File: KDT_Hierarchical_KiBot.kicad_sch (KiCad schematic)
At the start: 0 parts

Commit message: QR Code Added
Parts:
- added QR1: QR_Revision, ProjectQR:QR_Revision, symbol ProjectQR:QR_Revision
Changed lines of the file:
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@@
+		)
+	)
+	(symbol
+		(lib_id "ProjectQR:QR_Revision")
+		(at 209.55 269.24 0)
+		(unit 1)
+		(exclude_from_sim no)
+		(in_bom no)
+		(on_board yes)
+		(dnp no)
+		(fields_autoplaced yes)
+		(property "Reference" "QR1"
+			(at 209.55 256.54 0)
+			(effects
+				(font
+					(size 1.27 1.27)
+				)
+			)
+		)
+		(property "Value" "QR_Revision"
+			(at 209.55 259.08 0)
+			(effects
+				(font
+					(size 1.27 1.27)
+				)
+			)
+		)
+		(property "Footprint" "ProjectQR:QR_Revision"
+			(at 209.55 279.69 0)
+			(effects
+				(font
+					(size 1.27 1.27)
+				)
+				(hide yes)
+			)
+		)
+		(property "Datasheet" ""
+			(at 209.55 281.39 0)
+			(effects
+				(font
+					(size 1.27 1.27)
+				)
+				(hide yes)
+			)
+		)
+		(property "Description" ""
+			(at 209.55 269.24 0)
+			(effects
+				(font
+					(size 1.27 1.27)
+				)
+				(hide yes)
+			)
+		)
+		(property "qr_version" "2"
+			(at 209.55 283.09 0)
+			(effects
+				(font
+					(size 1.27 1.27)
+				)
+				(hide yes)
+			)
+		)
+		(property "qr_size" "25"
+			(at 209.55 284.79 0)
+			(effects
+				(font
+					(size 1.27 1.27)
+				)
+				(hide yes)
+			)
+		)
+		(property "qr_ecc" "2,3"
+			(at 209.55 286.49 0)
+			(effects
+				(font
+					(size 1.27 1.27)
+				)
+				(hide yes)
+			)
+		)
+		(property "qr_mask" "6"
+			(at 209.55 288.19 0)
+			(effects
+				(font
+					(size 1.27 1.27)
+				)
+				(hide yes)
+			)
+		)
+		(property "qr_text" "R1.4.2+ (Unreleased)"
+			(at 209.55 289.89 0)
+			(effects
+				(font
+					(size 1.27 1.27)
+				)
+				(hide yes)
+			)
+		)
+		(property "Sim.Enable" "0"
+			(at 209.55 291.59 0)
+			(effects
+				(font
+					(size 1.27 1.27)
+				)
+				(hide yes)
+			)
+		)
+		(instances
+			(project "KDT_Hierarchical_KiBot"
+				(path "/f9e05184-c88b-4a88-ae9c-ab2bdb32be7c"
+					(reference "QR1")
+					(unit 1)
+				)
+			)
 		)
 	)

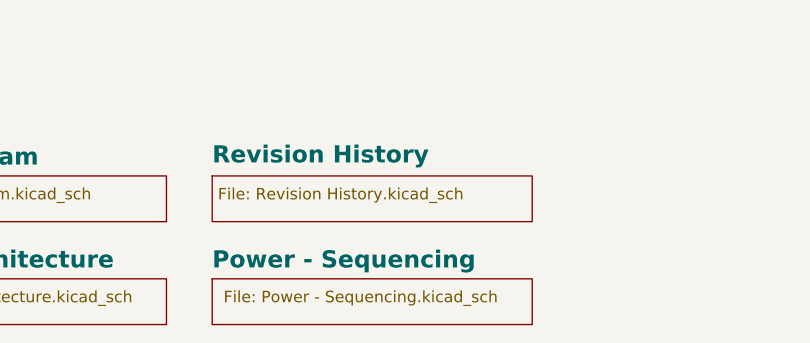
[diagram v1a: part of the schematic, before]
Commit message: Added conformal coat generation, removed KiRi to prevent bloat and dropped the power sequencing sheet
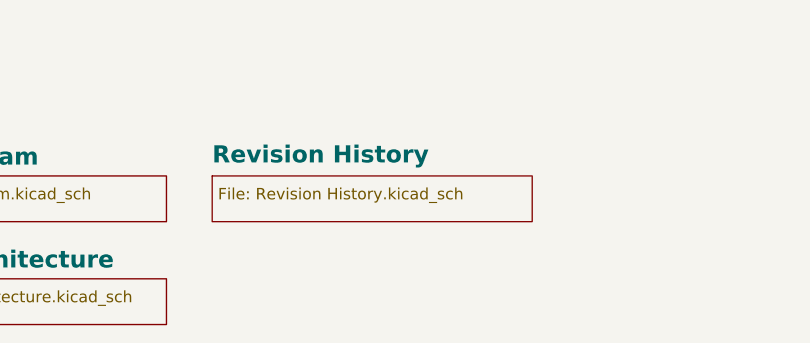
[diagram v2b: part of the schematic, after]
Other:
- removed sheet Power - Sequencing
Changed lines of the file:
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@@
 		(at 209.55 269.24 0)
 		(unit 1)
-		(exclude_from_sim no)
+		(exclude_from_sim yes)
 		(in_bom no)
 		(on_board yes)
@@
 			)
 		)
-		(property "Sim.Enable" "0"
-			(at 209.55 291.59 0)
-			(effects
-				(font
-					(size 1.27 1.27)
-				)
-				(hide yes)
-			)
-		)
 		(instances
 			(project "KDT_Hierarchical_KiBot"
@@
 					(reference "QR1")
 					(unit 1)
-				)
-			)
-		)
-	)
-	(sheet
-		(at 340.36 313.69)
-		(size 35.56 5.08)
-		(exclude_from_sim no)
-		(in_bom yes)
-		(on_board yes)
-		(dnp no)
-		(stroke
-			(width 0.1524)
-			(type solid)
-		)
-		(fill
-			(color 0 0 0 0.0000)
-		)
-		(property "Sheetname" "Power - Sequencing"
-			(at 340.36 312.6609 0)
-			(effects
-				(font
-					(face "Times New Roman")
-					(size 1.905 1.905)
-					(bold yes)
-					(color 0 0 0 1)
-				)
-				(justify left bottom)
-			)
-		)
-		(property "Sheetfile" "Power - Sequencing.kicad_sch"
-			(at 341.63 314.96 0)
-			(effects
-				(font
-					(face "Arial")
-					(size 1.27 1.27)
-				)
-				(justify left top)
-			)
-		)
-		(instances
-			(project "KDT_Hierarchical_KiBot"
-				(path "/f9e05184-c88b-4a88-ae9c-ab2bdb32be7c"
-					(page "6")
 				)
 			)
@@
 			(project "KDT_Hierarchical_KiBot"
 				(path "/f9e05184-c88b-4a88-ae9c-ab2bdb32be7c"
-					(page "7")
+					(page "6")
 				)
 			)
